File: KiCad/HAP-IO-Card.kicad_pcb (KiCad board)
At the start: 2 copper layers, 110 x 72 mm, 418 parts, among them CON601 AVR-JTAG-10, J201 TE_Connectivity_1-282834-0, J202 TE_Connectivity_282834-6, J203 GS3, J204 GS3, J205 GS3, J206 GS3, J207 GS3, J208 GS3, J209 GS3, J210 GS3, J211 TE_Connectivity_282834-6, J212 TE_Connectivity_1-282834-0, J401 TE_Connectivity_1-282834-0, J402 TE_Connectivity_282834-6, J501 TE_Connectivity_282834-3, J502 CONN_01X03_FEMALE, J601 ISP0, J602 ISP1, J603 CONN_01X02, J604 CONN_01X02, J605 CONN_01X02, J606 CONN_01X02, J607 CONN_01X03, J608 CONN_01X03, J701 5V_I/O_2, J702 5V_I/O_1, J703 NEO1, J704 NEO2, J705 NEO3, J706 NEO4, J707 CONN_01X03, Q201 ZXTN25050DFHTA, Q202 ZXTN25050DFHTA, Q203 ZXTN25050DFHTA, Q204 ZXTN25050DFHTA, Q205 ZXTN25050DFHTA, Q206 ZXTN25050DFHTA, Q207 ZXTN25050DFHTA, Q208 ZXTN25050DFHTA, U201 LTV-354T, U202 LTV-354T, U203 LTV-354T, U204 LTV-354T, U205 LTV-354T, U206 LTV-354T, U207 LTV-354T, U208 LTV-354T, U209 MCP23017, U401 ADS1115IDGST, U402 ADS1115IDGST, U501 LM1086-5V, U502 LM1086-3.3V, U701 TXB0102DCT

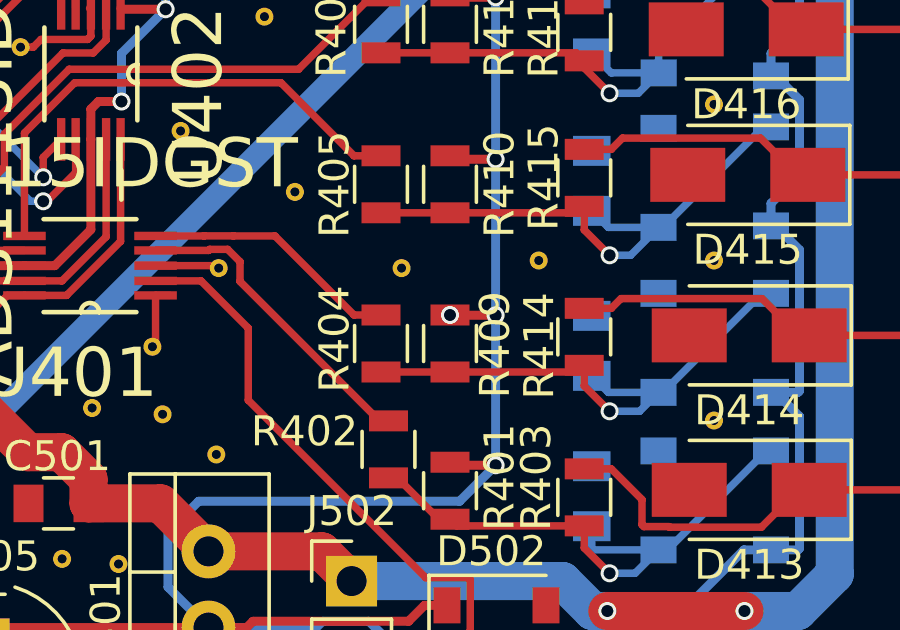
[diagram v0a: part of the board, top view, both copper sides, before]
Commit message: Removed via in pad
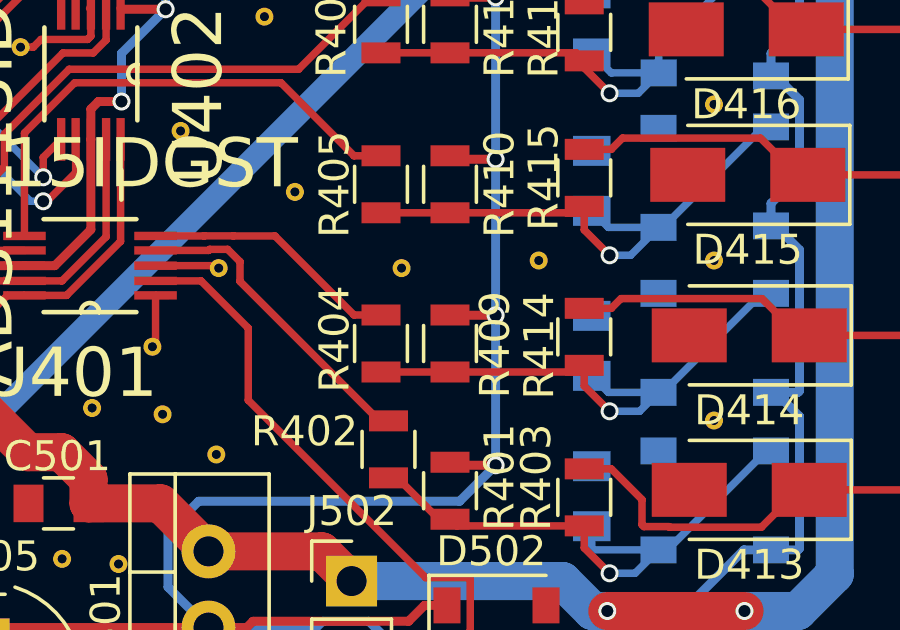
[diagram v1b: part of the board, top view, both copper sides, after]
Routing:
- net POWER5V: vias 15 -> 14
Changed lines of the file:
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@@
   (general
     (links 665)
-    (no_connects 3)
+    (no_connects 1)
     (area 34.499762 14.857666 147.875572 90.7625)
     (thickness 1.6)
     (drawings 198)
-    (tracks 1850)
+    (tracks 1849)
     (zones 0)
     (modules 418)
@@
   (segment (start 124.8 73.2) (end 123.289146 73.2) (width 0.3) (layer F.Cu) (net 32) (status 20))
   (segment (start 123.289146 73.2) (end 123.28 73.190854) (width 0.3) (layer F.Cu) (net 32) (status 30))
-  (via (at 123.28 73.190854) (size 0.6) (drill 0.4) (layers F.Cu B.Cu) (net 32) (status 30))
   (segment (start 124.8 78.2) (end 124.8 73.2) (width 0.3) (layer B.Cu) (net 32))
   (via (at 124.8 73.2) (size 0.6) (drill 0.4) (layers F.Cu B.Cu) (net 32))

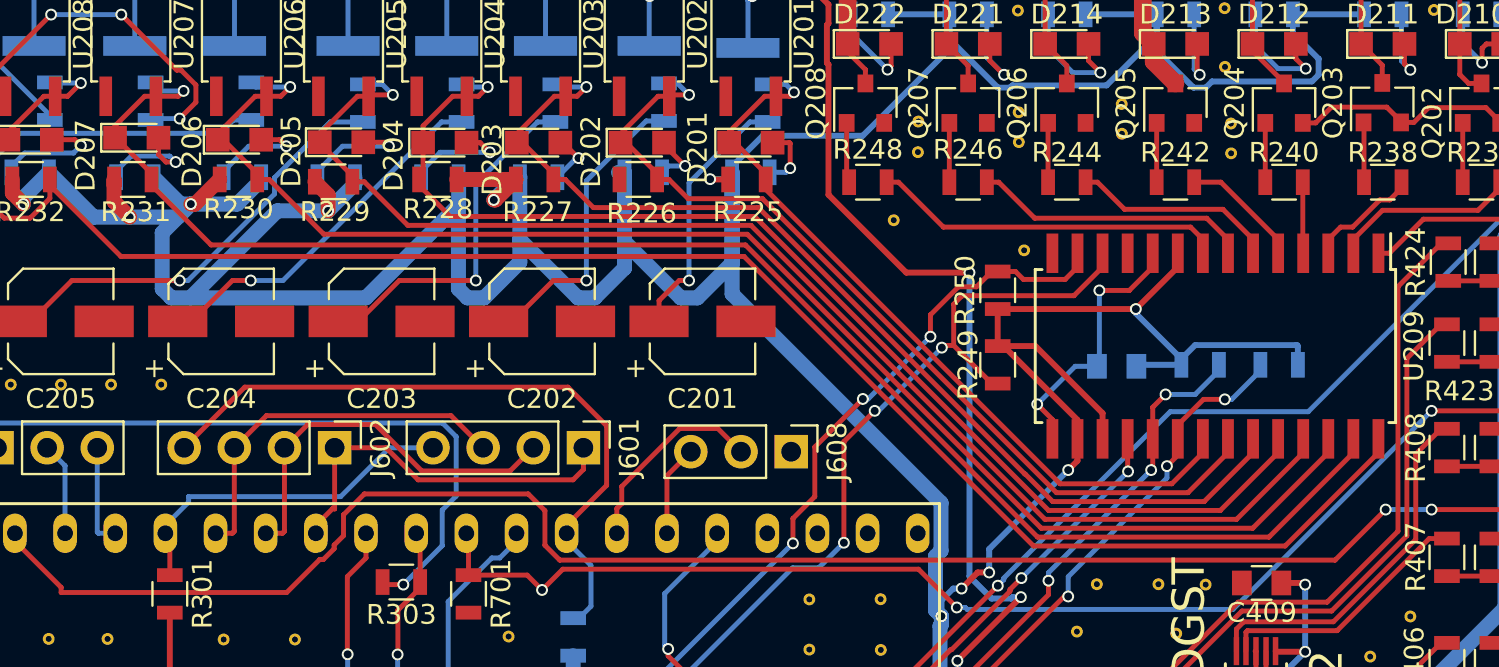
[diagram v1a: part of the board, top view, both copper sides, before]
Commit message: Fixed unconnected pad
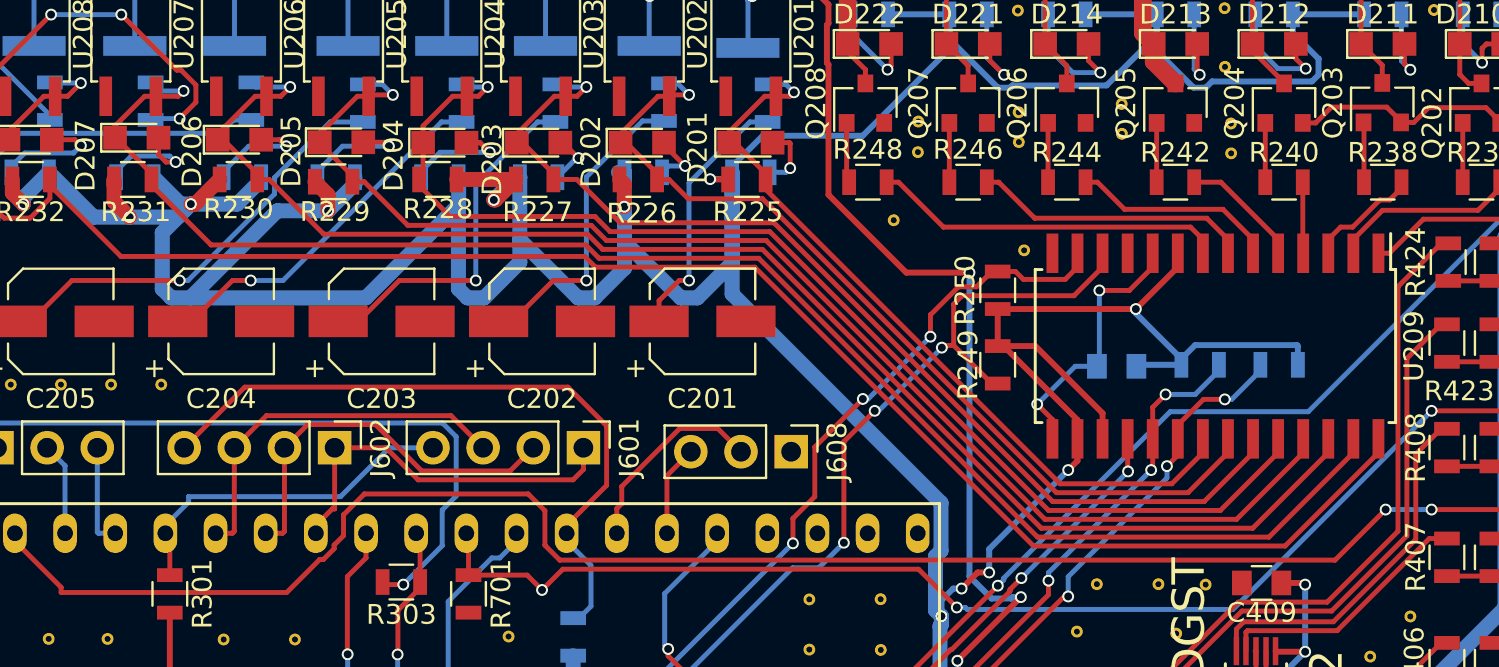
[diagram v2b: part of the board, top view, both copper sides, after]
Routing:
- net POWER3V3: track 529.3 -> 532.5 mm, vias 21 -> 22

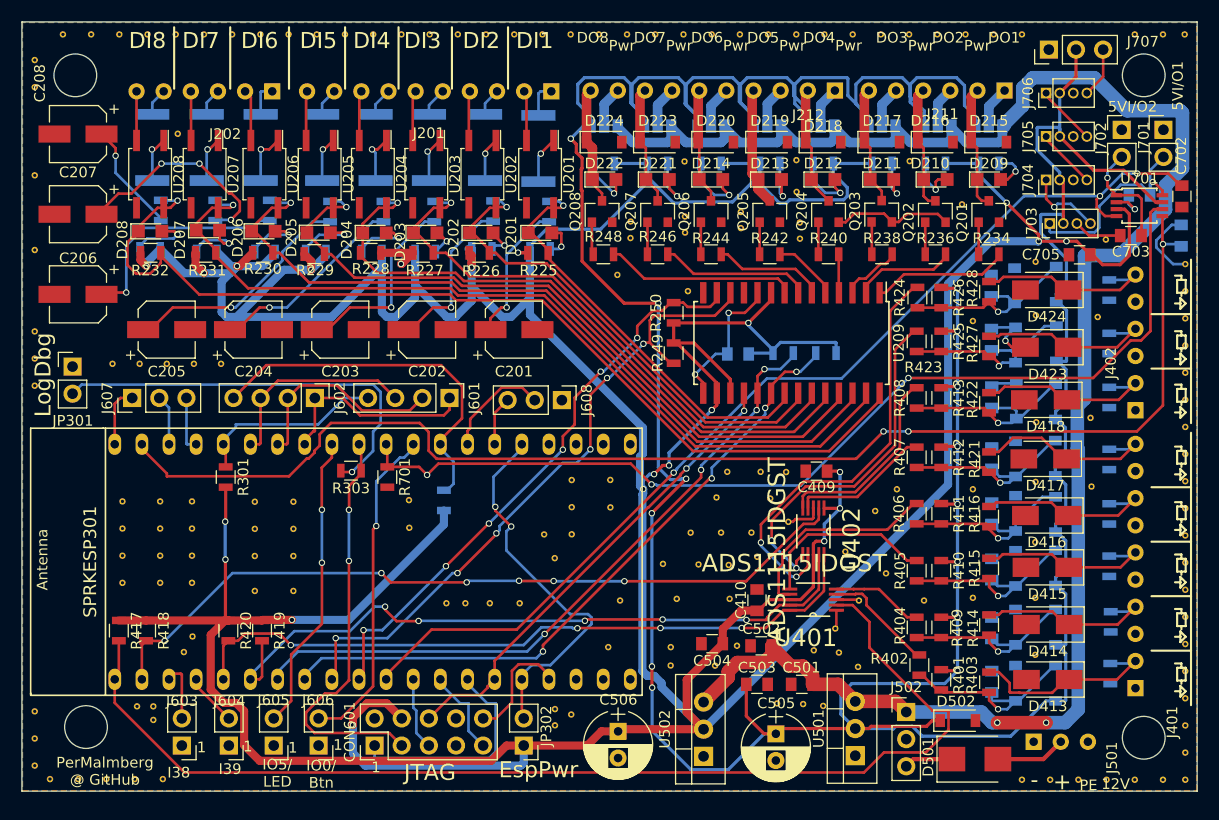
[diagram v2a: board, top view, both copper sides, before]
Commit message: Increased size of some 3.3V wires
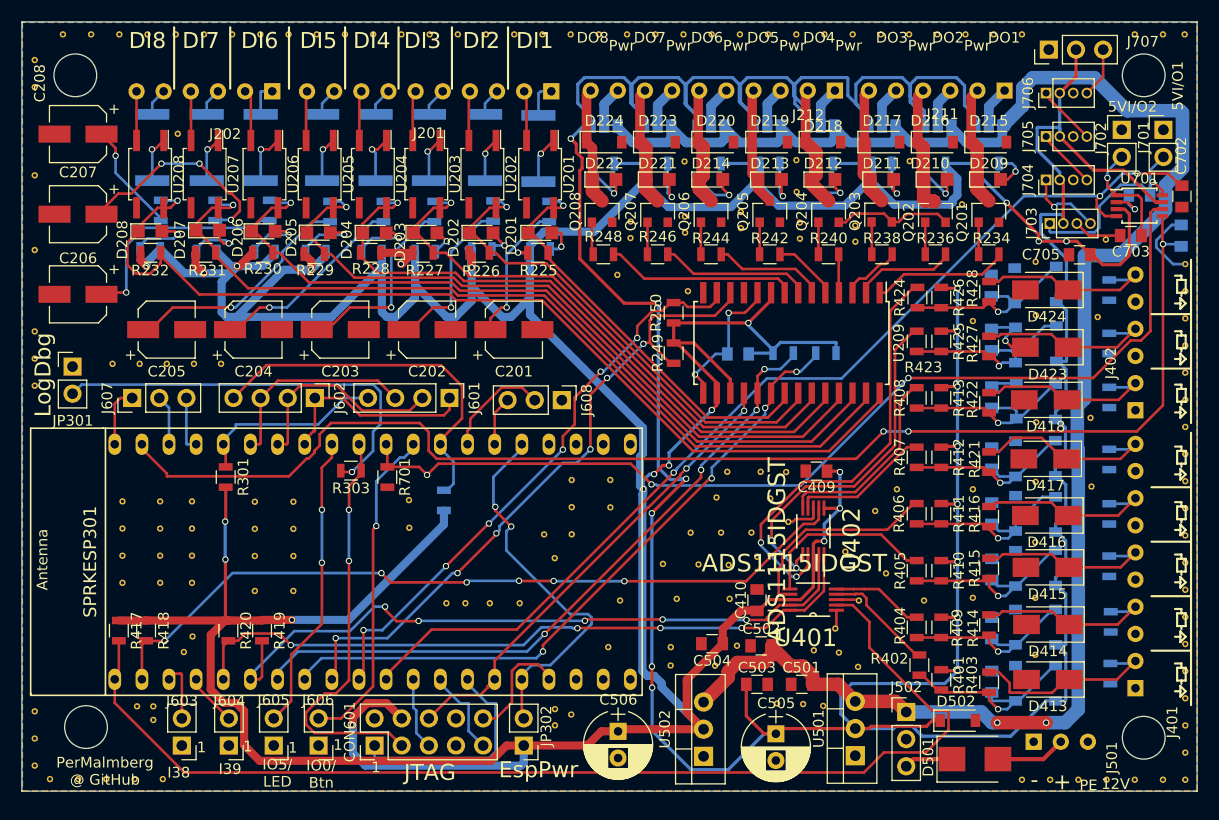
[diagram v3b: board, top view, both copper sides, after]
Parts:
- added REF**: StichingVia, StichingVIA:StichingVia, F.Cu at (115.2, 38.0)
- added REF**: StichingVia, StichingVIA:StichingVia, F.Cu at (115.2, 36.5)
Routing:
- net POWER3V3: track 532.5 -> 487.8 mm
- net /Digital I/O/DO_4: track 11.3 -> 12.1 mm

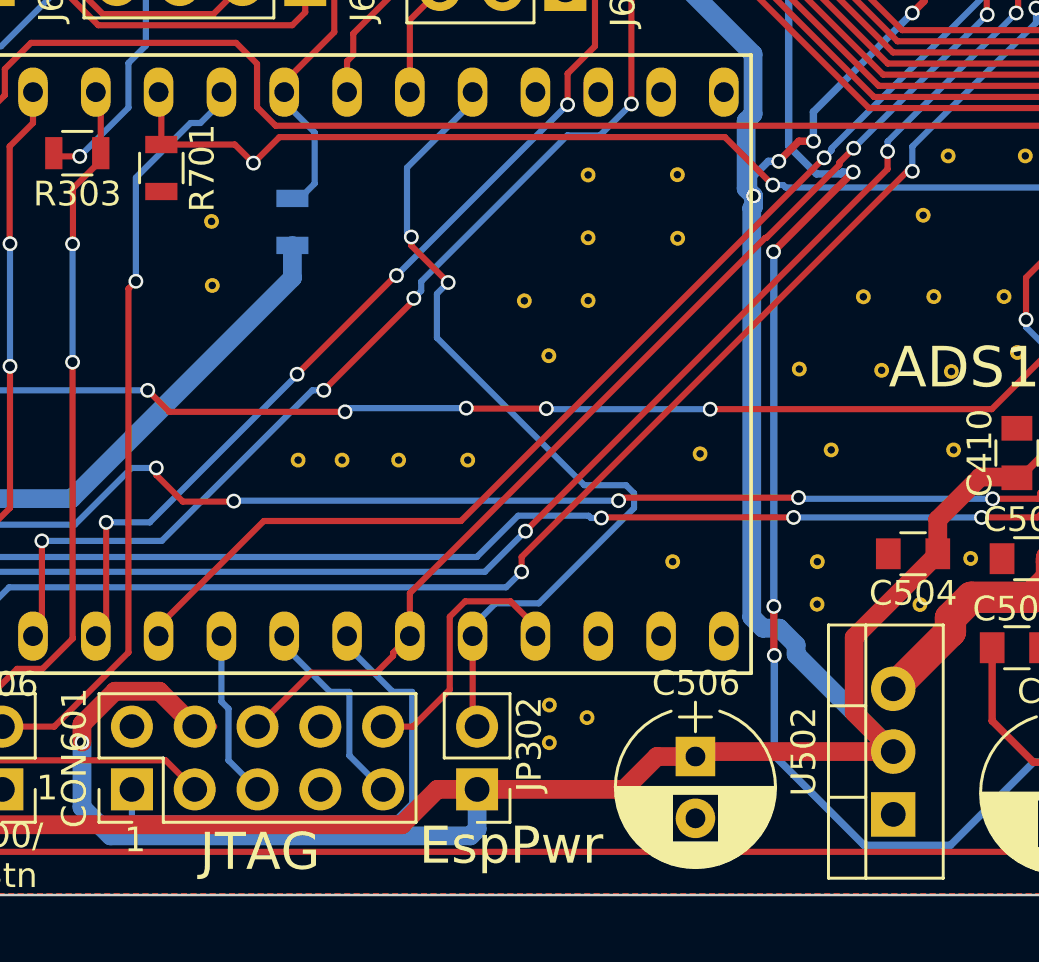
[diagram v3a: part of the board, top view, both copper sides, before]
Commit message: Added pullups for JTAG
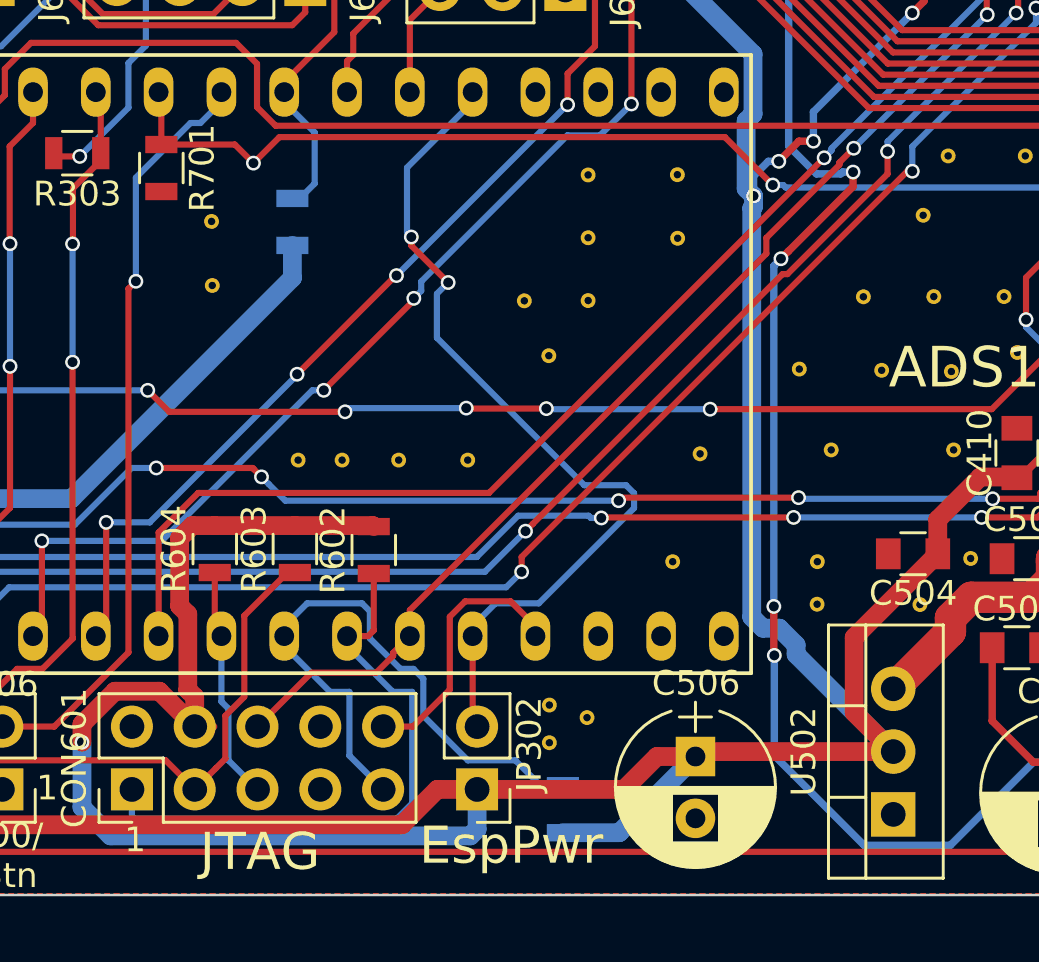
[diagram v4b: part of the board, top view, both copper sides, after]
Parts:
- added R601: 10k, Resistors_SMD:R_0805, B.Cu at (87.7, 86.0)
- added R602: 10k, Resistors_SMD:R_0805, F.Cu at (80.0, 75.5)
- added R603: 10k, Resistors_SMD:R_0805, F.Cu at (76.8, 75.5)
- added R604: 10k, Resistors_SMD:R_0805, F.Cu at (73.6, 75.5)
- C701, C702, C703, C704, C705: value 100nF -> 100n
- J701: value 5V_I/O_2 -> 5V_I/O_1
- J702: value 5V_I/O_1 -> 5V_I/O_2
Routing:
- net POWER3V3: track 487.8 -> 510.4 mm
- net JTAG:MTDI: track 8.31 -> 24.9 mm
- net JTAG:MTDO: track 38.8 -> 49.5 mm
- net JTAG:MTCK: track 21.0 -> 24.5 mm
- net JTAG:MTMS: track 6.80 -> 9.49 mm
- net 5V_IO_2: track 98.4 -> 100.6 mm
